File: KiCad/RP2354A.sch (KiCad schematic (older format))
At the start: 21 parts, among them J11 Conn_01x02, J16 USB_C_Receptacle_USB2.0, U16 RP2354A, Y1 ABM8-272-T3

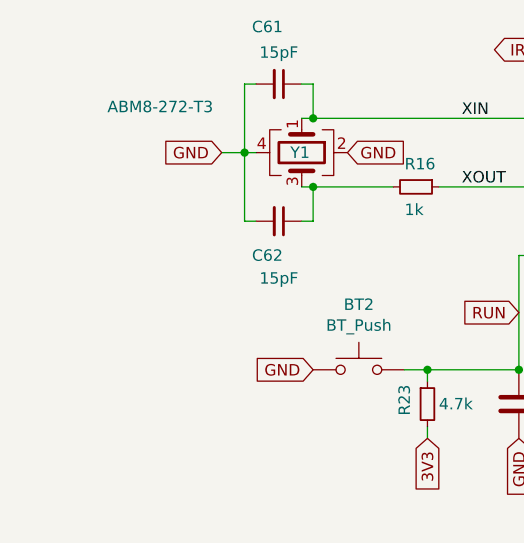
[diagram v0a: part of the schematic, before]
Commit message: Add debug header (SWCLK,GND,SWDIO) for the RP2354A as a standard 2.54 mm pin pitch three-pin header
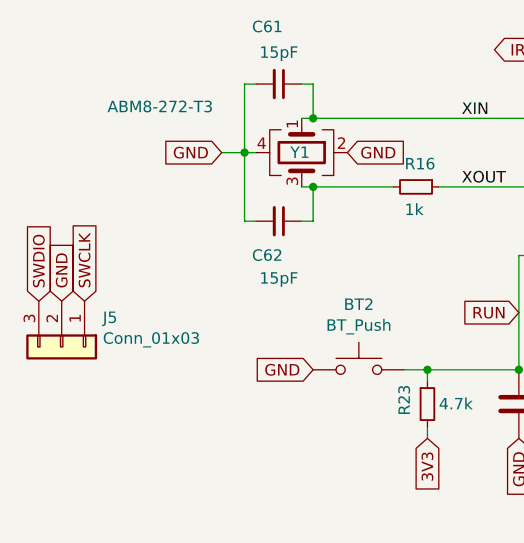
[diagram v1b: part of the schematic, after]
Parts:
- added J5: Conn_01x03, Connector_PinHeader_2.54mm:PinHeader_1x03_P2.54mm_Vertical, symbol Connector_Generic:Conn_01x03
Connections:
- net GND: now also J5.2 (Pin_2)
- net SWCLK: now also J5.1 (Pin_1)
- net SWDIO: now also J5.3 (Pin_3)
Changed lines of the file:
@@
 Text GLabel 3300 4500 3    50   Input ~ 0
 GND
+$Comp
+L Connector_Generic:Conn_01x03 J5
+U 1 1 6B3FC5A9
+P 1300 4100
+F 0 "J5" V 1172 4280 50  0000 L CNN
+F 1 "Conn_01x03" V 1263 4280 50  0000 L CNN
+F 2 "Connector_PinHeader_2.54mm:PinHeader_1x03_P2.54mm_Vertical" H 1300 4100 50  0001 C CNN
+F 3 "~" H 1300 4100 50  0001 C CNN
+	1    1300 4100
+	0    1    1    0
+$EndComp
+Text GLabel 1400 3900 1    50   Input ~ 0
+SWCLK
+Text GLabel 1200 3900 1    50   Input ~ 0
+SWDIO
+Text GLabel 1300 3900 1    50   Input ~ 0
+GND
 $EndSCHEMATC

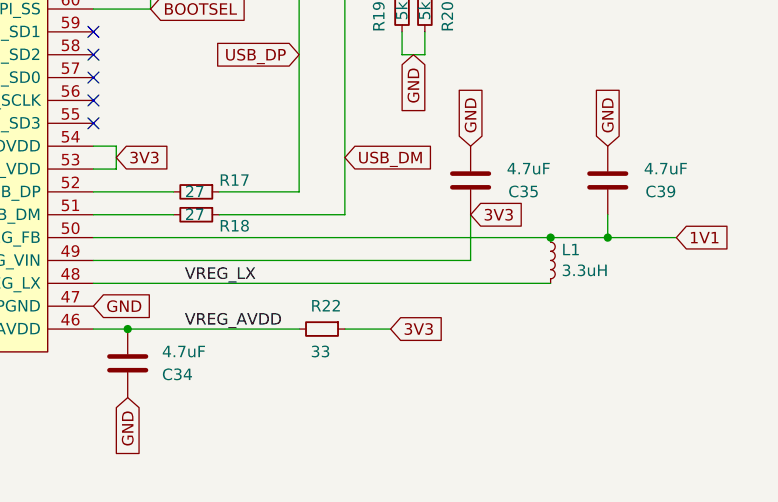
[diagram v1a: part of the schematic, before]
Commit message: Change C19 reference to C39, Change C18 reference to C35, Change C17 reference to C34, Change C16 reference to C19, Change C15 reference to C18, Change C14 reference to C17, Change C13 reference to C16, Change C11 reference to C15, Change C12 reference to C14, Change C10 reference to C13, Change C9 reference to C12, Change C39 reference to C11, Change C35 reference to C10, Change C34 reference to C9.
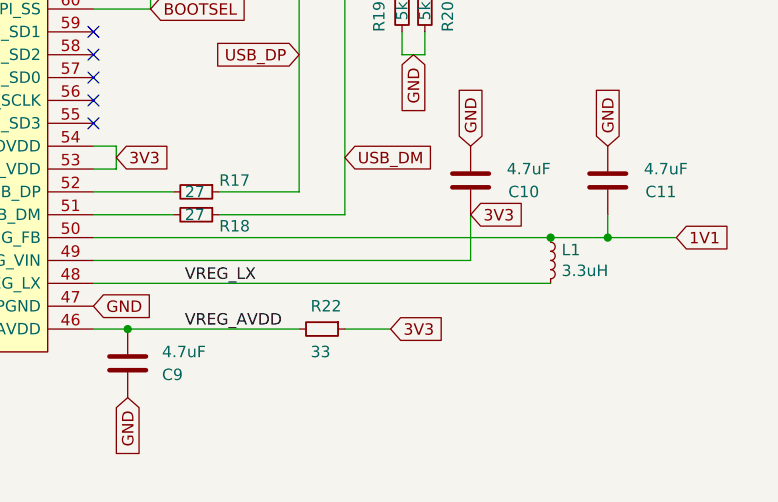
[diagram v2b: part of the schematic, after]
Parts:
- renumbered C35 to C10, C39 to C11, C34 to C9
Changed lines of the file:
@@
 P 7050 4350
 AR Path="/6AF78685" Ref="C?"  Part="1"
-AR Path="/6AFE5B10/6AF78685" Ref="C34"  Part="1"
-F 0 "C34" H 7200 4300 50  0000 L CNN
+AR Path="/6AFE5B10/6AF78685" Ref="C9"  Part="1"
+F 0 "C9" H 7200 4300 50  0000 L CNN
 F 1 "4.7uF" H 7200 4400 50  0000 L CNN
 F 2 "Capacitor_SMD:C_1206_3216Metric_Pad1.33x1.80mm_HandSolder" H 7088 4200 50  0001 C CNN
@@
 P 8550 3550
 AR Path="/6AF91B11" Ref="C?"  Part="1"
-AR Path="/6AFE5B10/6AF91B11" Ref="C35"  Part="1"
-F 0 "C35" H 8250 3600 50  0000 L CNN
+AR Path="/6AFE5B10/6AF91B11" Ref="C10"  Part="1"
+F 0 "C10" H 8250 3600 50  0000 L CNN
 F 1 "4.7uF" H 8200 3500 50  0000 L CNN
 F 2 "Capacitor_SMD:C_1206_3216Metric_Pad1.33x1.80mm_HandSolder" H 8588 3400 50  0001 C CNN
@@
 P 9150 3550
 AR Path="/6AFADC4E" Ref="C?"  Part="1"
-AR Path="/6AFE5B10/6AFADC4E" Ref="C39"  Part="1"
-F 0 "C39" H 8850 3600 50  0000 L CNN
+AR Path="/6AFE5B10/6AFADC4E" Ref="C11"  Part="1"
+F 0 "C11" H 8850 3600 50  0000 L CNN
 F 1 "4.7uF" H 8800 3500 50  0000 L CNN
 F 2 "Capacitor_SMD:C_1206_3216Metric_Pad1.33x1.80mm_HandSolder" H 9188 3400 50  0001 C CNN

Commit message: Change C38 reference to C48, Change C40 reference to C47, Change C48 reference to C44, Change C44 reference to C43, Change C43 reference to C42, Change C42 reference to C41, Change C41 reference to C40, Change C47 reference to C39, Change C39 reference to C38.
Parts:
- renumbered C40 to C47
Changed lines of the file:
@@
 	2900 4450 2900 4500
 $Comp
-L Device:C C40
+L Device:C C47
 U 1 1 6B09868D
 P 3300 4350
-F 0 "C40" H 3350 4450 50  0000 L CNN
+F 0 "C47" H 3350 4450 50  0000 L CNN
 F 1 "0.1uF" H 3350 4250 50  0000 L CNN
 F 2 "Capacitor_SMD:C_0603_1608Metric_Pad1.08x0.95mm_HandSolder" H 3338 4200 50  0001 C CNN

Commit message: Change C54 reference to C62, Change C53 reference to C61, Change C52 reference to C60, Change C51 reference to C59, Change C50 reference to C58, Change C49 reference to C57, Change C60 reference to C56, Change C59 reference to C55, Change C58 reference to C54, Change C57 reference to C53, Change C56 reference to C52, Change C55 reference to C51, Change C62 reference to C50, Change C61 reference to C49.
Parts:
- renumbered C61 to C49, C62 to C50
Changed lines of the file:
@@
 	3350 3300 3350 3400
 $Comp
-L Device:C_Small C61
+L Device:C_Small C49
 U 1 1 6B2625A2
 P 2250 2950
-F 0 "C61" V 2000 2900 50  0000 C CNN
+F 0 "C49" V 2000 2900 50  0000 C CNN
 F 1 "15pF" V 2112 2950 50  0000 C CNN
 F 2 "Capacitor_SMD:C_0603_1608Metric_Pad1.08x0.95mm_HandSolder" H 2250 2950 50  0001 C CNN
@@
 $EndComp
 $Comp
-L Device:C_Small C62
+L Device:C_Small C50
 U 1 1 6B263398
 P 2250 3550
-F 0 "C62" V 2400 3500 50  0000 C CNN
+F 0 "C50" V 2400 3500 50  0000 C CNN
 F 1 "15pF" V 2500 3550 50  0000 C CNN
 F 2 "Capacitor_SMD:C_0603_1608Metric_Pad1.08x0.95mm_HandSolder" H 2250 3550 50  0001 C CNN

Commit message: Change C45 reference to C48, Change C44 reference to C47, Change C48 reference to C45, Change C47 reference to C44.
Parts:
- renumbered C47 to C44
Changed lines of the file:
@@
 	2900 4450 2900 4500
 $Comp
-L Device:C C47
+L Device:C C44
 U 1 1 6B09868D
 P 3300 4350
-F 0 "C47" H 3350 4450 50  0000 L CNN
+F 0 "C44" H 3350 4450 50  0000 L CNN
 F 1 "0.1uF" H 3350 4250 50  0000 L CNN
 F 2 "Capacitor_SMD:C_0603_1608Metric_Pad1.08x0.95mm_HandSolder" H 3338 4200 50  0001 C CNN

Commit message: Change R8 reference to R11, Change R11 reference to R8, Change R11 reference to R21,Change R10 reference to R11,Change R9 reference to R10,Change R21 reference to R9.
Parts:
- renumbered R21 to R9
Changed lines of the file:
@@
 P 6900 2300
 AR Path="/6AE48264" Ref="R?"  Part="1"
-AR Path="/6AFE5B10/6AE48264" Ref="R21"  Part="1"
-F 0 "R21" V 6800 2250 50  0000 L CNN
+AR Path="/6AFE5B10/6AE48264" Ref="R9"  Part="1"
+F 0 "R9" V 6800 2250 50  0000 L CNN
 F 1 "1k" V 7000 2250 50  0000 L CNN
 F 2 "Resistor_SMD:R_0603_1608Metric_Pad0.98x0.95mm_HandSolder" H 6900 2300 50  0001 C CNN

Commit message: Change R11 reference to R18, Change R10 reference to R17, Change R9 reference to R11, Change R18 reference to R10, Change R17 reference to R9.
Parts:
- renumbered R18 to R10, R9 to R11, R17 to R9
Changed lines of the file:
@@
 Text GLabel 7150 2800 2    50   Input ~ 0
 BOOTSEL
-$Comp
-L Device:R_Small R?
-U 1 1 6ADC9F07
-P 7350 3600
-AR Path="/6ADC9F07" Ref="R?"  Part="1"
-AR Path="/6AFE5B10/6ADC9F07" Ref="R17"  Part="1"
-F 0 "R17" V 7300 3700 50  0000 L CNN
-F 1 "27" V 7350 3550 50  0000 L CNN
-F 2 "Resistor_SMD:R_0603_1608Metric_Pad0.98x0.95mm_HandSolder" H 7350 3600 50  0001 C CNN
-F 3 "~" H 7350 3600 50  0001 C CNN
-	1    7350 3600
-	0    1    1    0
-$EndComp
 Wire Wire Line
 	6900 3600 7250 3600
-$Comp
-L Device:R_Small R?
-U 1 1 6ADD8B0E
-P 7350 3700
-AR Path="/6ADD8B0E" Ref="R?"  Part="1"
-AR Path="/6AFE5B10/6ADD8B0E" Ref="R18"  Part="1"
-F 0 "R18" V 7400 3800 50  0000 L CNN
-F 1 "27" V 7350 3650 50  0000 L CNN
-F 2 "Resistor_SMD:R_0603_1608Metric_Pad0.98x0.95mm_HandSolder" H 7350 3700 50  0001 C CNN
-F 3 "~" H 7350 3700 50  0001 C CNN
-	1    7350 3700
-	0    1    1    0
-$EndComp
 Wire Wire Line
 	6900 3700 7250 3700
@@
 P 6900 2300
 AR Path="/6AE48264" Ref="R?"  Part="1"
-AR Path="/6AFE5B10/6AE48264" Ref="R9"  Part="1"
-F 0 "R9" V 6800 2250 50  0000 L CNN
+AR Path="/6AFE5B10/6AE48264" Ref="R11"  Part="1"
+F 0 "R11" V 6800 2250 50  0000 L CNN
 F 1 "1k" V 7000 2250 50  0000 L CNN
 F 2 "Resistor_SMD:R_0603_1608Metric_Pad0.98x0.95mm_HandSolder" H 6900 2300 50  0001 C CNN
@@
 Text GLabel 1300 3900 1    50   Input ~ 0
 GND
+$Comp
+L Device:R_Small R?
+U 1 1 6ADC9F07
+P 7350 3600
+AR Path="/6ADC9F07" Ref="R?"  Part="1"
+AR Path="/6AFE5B10/6ADC9F07" Ref="R9"  Part="1"
+F 0 "R9" V 7300 3700 50  0000 L CNN
+F 1 "27" V 7350 3550 50  0000 L CNN
+F 2 "Resistor_SMD:R_0603_1608Metric_Pad0.98x0.95mm_HandSolder" H 7350 3600 50  0001 C CNN
+F 3 "~" H 7350 3600 50  0001 C CNN
+	1    7350 3600
+	0    1    1    0
+$EndComp
+$Comp
+L Device:R_Small R?
+U 1 1 6ADD8B0E
+P 7350 3700
+AR Path="/6ADD8B0E" Ref="R?"  Part="1"
+AR Path="/6AFE5B10/6ADD8B0E" Ref="R10"  Part="1"
+F 0 "R10" V 7400 3800 50  0000 L CNN
+F 1 "27" V 7350 3650 50  0000 L CNN
+F 2 "Resistor_SMD:R_0603_1608Metric_Pad0.98x0.95mm_HandSolder" H 7350 3700 50  0001 C CNN
+F 3 "~" H 7350 3700 50  0001 C CNN
+	1    7350 3700
+	0    1    1    0
+$EndComp
 $EndSCHEMATC

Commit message: Change R14 reference to R23, Change R13 reference to R22, Change R12 reference to R20, Change R15 reference to R19, Change R20 reference to R16, Change R19 reference to R15, Change R23 reference to R14, Change R11 reference to R13, Change R16 reference to R12, Change R22 reference to R11.
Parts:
- renumbered R22 to R11, R16 to R12, R11 to R13, R23 to R14, R19 to R15, R20 to R16
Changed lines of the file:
@@
 P 2850 3400
 AR Path="/6B28DDCB" Ref="R?"  Part="1"
-AR Path="/6AFE5B10/6B28DDCB" Ref="R16"  Part="1"
-F 0 "R16" V 2750 3350 50  0000 L CNN
+AR Path="/6AFE5B10/6B28DDCB" Ref="R12"  Part="1"
+F 0 "R12" V 2750 3350 50  0000 L CNN
 F 1 "1k" V 2950 3350 50  0000 L CNN
 F 2 "Resistor_SMD:R_0603_1608Metric_Pad0.98x0.95mm_HandSolder" H 2850 3400 50  0001 C CNN
@@
 Text GLabel 7050 1700 0    50   Input ~ 0
 GND
-$Comp
-L Device:R_Small R19
-U 1 1 6AE0E7AA
-P 8250 2800
-F 0 "R19" V 8150 2700 50  0000 L CNN
-F 1 "5k1" V 8250 2750 50  0000 L CNN
-F 2 "Resistor_SMD:R_0603_1608Metric_Pad0.98x0.95mm_HandSolder" H 8250 2800 50  0001 C CNN
-F 3 "~" H 8250 2800 50  0001 C CNN
-	1    8250 2800
-	1    0    0    -1
-$EndComp
 Wire Wire Line
 	8250 2600 8250 2700
@@
 Text GLabel 8300 3000 3    50   Input ~ 0
 GND
-$Comp
-L Device:R_Small R20
-U 1 1 6AE0E7B3
-P 8350 2800
-F 0 "R20" V 8450 2700 50  0000 L CNN
-F 1 "5k1" V 8350 2750 50  0000 L CNN
-F 2 "Resistor_SMD:R_0603_1608Metric_Pad0.98x0.95mm_HandSolder" H 8350 2800 50  0001 C CNN
-F 3 "~" H 8350 2800 50  0001 C CNN
-	1    8350 2800
-	1    0    0    -1
-$EndComp
 Wire Wire Line
 	8350 2600 8350 2700
@@
 P 6900 2300
 AR Path="/6AE48264" Ref="R?"  Part="1"
-AR Path="/6AFE5B10/6AE48264" Ref="R11"  Part="1"
-F 0 "R11" V 6800 2250 50  0000 L CNN
+AR Path="/6AFE5B10/6AE48264" Ref="R13"  Part="1"
+F 0 "R13" V 6800 2250 50  0000 L CNN
 F 1 "1k" V 7000 2250 50  0000 L CNN
 F 2 "Resistor_SMD:R_0603_1608Metric_Pad0.98x0.95mm_HandSolder" H 6900 2300 50  0001 C CNN
@@
 P 7900 4200
 AR Path="/6AFDAD5A" Ref="R?"  Part="1"
-AR Path="/6AFE5B10/6AFDAD5A" Ref="R22"  Part="1"
-F 0 "R22" V 7800 4150 50  0000 L CNN
+AR Path="/6AFE5B10/6AFDAD5A" Ref="R11"  Part="1"
+F 0 "R11" V 7800 4150 50  0000 L CNN
 F 1 "33" V 8000 4150 50  0000 L CNN
 F 2 "Resistor_SMD:R_0603_1608Metric_Pad0.98x0.95mm_HandSolder" H 7900 4200 50  0001 C CNN
@@
 P 2900 4350
 AR Path="/6B05EE3D" Ref="R?"  Part="1"
-AR Path="/6AFE5B10/6B05EE3D" Ref="R23"  Part="1"
-F 0 "R23" V 2800 4300 50  0000 L CNN
+AR Path="/6AFE5B10/6B05EE3D" Ref="R14"  Part="1"
+F 0 "R14" V 2800 4300 50  0000 L CNN
 F 1 "4.7k" H 2950 4350 50  0000 L CNN
 F 2 "Resistor_SMD:R_0603_1608Metric_Pad0.98x0.95mm_HandSolder" H 2900 4350 50  0001 C CNN
@@
 	0    1    1    0
 $EndComp
+$Comp
+L Device:R_Small R15
+U 1 1 6AE0E7AA
+P 8250 2800
+F 0 "R15" V 8150 2700 50  0000 L CNN
+F 1 "5k1" V 8250 2750 50  0000 L CNN
+F 2 "Resistor_SMD:R_0603_1608Metric_Pad0.98x0.95mm_HandSolder" H 8250 2800 50  0001 C CNN
+F 3 "~" H 8250 2800 50  0001 C CNN
+	1    8250 2800
+	1    0    0    -1
+$EndComp
+$Comp
+L Device:R_Small R16
+U 1 1 6AE0E7B3
+P 8350 2800
+F 0 "R16" V 8450 2700 50  0000 L CNN
+F 1 "5k1" V 8350 2750 50  0000 L CNN
+F 2 "Resistor_SMD:R_0603_1608Metric_Pad0.98x0.95mm_HandSolder" H 8350 2800 50  0001 C CNN
+F 3 "~" H 8350 2800 50  0001 C CNN
+	1    8350 2800
+	1    0    0    -1
+$EndComp
 $EndSCHEMATC
